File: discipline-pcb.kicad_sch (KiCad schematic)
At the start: 143 parts, among them SW1 KEYSW, SW10 KEYSW, SW11 KEYSW, SW12 KEYSW, SW13 KEYSW, SW14 KEYSW, SW16 KEYSW, SW17 KEYSW, SW18 KEYSW, SW19 KEYSW, SW2 KEYSW, SW20 KEYSW, SW21 KEYSW, SW22 KEYSW, SW23 KEYSW, SW24 KEYSW, SW25 KEYSW, SW26 KEYSW, SW27 KEYSW, SW28 KEYSW, SW29 KEYSW, SW3 KEYSW, SW31 KEYSW, SW32 KEYSW, SW33 KEYSW, SW34 KEYSW, SW35 KEYSW, SW36 KEYSW, SW37 KEYSW, SW38 KEYSW, SW39 KEYSW, SW4 KEYSW, SW40 KEYSW, SW41 KEYSW, SW42 KEYSW, SW43 KEYSW, SW45 KEYSW, SW46 KEYSW, SW47 KEYSW, SW48 KEYSW, SW49 KEYSW, SW5 KEYSW, SW50 KEYSW, SW51 KEYSW, SW52 KEYSW, SW53 KEYSW, SW54 KEYSW, SW55 KEYSW, SW56 KEYSW, SW57 KEYSW, SW59 KEYSW, SW6 KEYSW, SW60 KEYSW, SW61 KEYSW, SW62 KEYSW, SW7 KEYSW, SW72 KEYSW, SW73 KEYSW, SW74 KEYSW, SW75 KEYSW, SW76 KEYSW, SW77 KEYSW, SW78 KEYSW, SW79 KEYSW, SW8 KEYSW, SW80 KEYSW, SW81 KEYSW, SW82 KEYSW, SW83 KEYSW, SW9 KEYSW

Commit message: add dru
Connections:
- net col0: now also A1.20 (GPIO15); no longer A1.26 (GPIO20)
- net col1: now also A1.19 (GPIO14); no longer A1.25 (GPIO19)
- net col10: now also A1.7 (GPIO5); no longer A1.14 (GPIO10)
- net col11: now also A1.6 (GPIO4); no longer A1.12 (GPIO9)
- net col12: now also A1.5 (GPIO3); no longer A1.11 (GPIO8)
- net col13: now also A1.21 (GPIO16); no longer A1.10 (GPIO7)
- net col14: now also A1.4 (GPIO2); no longer A1.9 (GPIO6)
- net col15: now also A1.2 (GPIO1); no longer A1.7 (GPIO5)
- net col16: now also A1.1 (GPIO0); no longer A1.6 (GPIO4)
- net col2: now also A1.17 (GPIO13); no longer A1.24 (GPIO18)
- net col3: now also A1.16 (GPIO12); no longer A1.22 (GPIO17)
- net col4: now also A1.15 (GPIO11); no longer A1.21 (GPIO16)
- net col5: now also A1.14 (GPIO10); no longer A1.20 (GPIO15)
- net col6: now also A1.12 (GPIO9); no longer A1.19 (GPIO14)
- net col7: now also A1.11 (GPIO8); no longer A1.17 (GPIO13)
- net col8: now also A1.10 (GPIO7); no longer A1.16 (GPIO12)
- net col9: now also A1.9 (GPIO6); no longer A1.15 (GPIO11)
- net row0: now also A1.32 (GPIO27_ADC1); no longer A1.34 (GPIO28_ADC2)
- net row1: now also A1.31 (GPIO26_ADC0); no longer A1.32 (GPIO27_ADC1)
- net row2: now also A1.27 (GPIO21); no longer A1.31 (GPIO26_ADC0)
- net row3: now also A1.34 (GPIO28_ADC2); no longer A1.29 (GPIO22)
- net row4: now also A1.29 (GPIO22); no longer A1.27 (GPIO21)

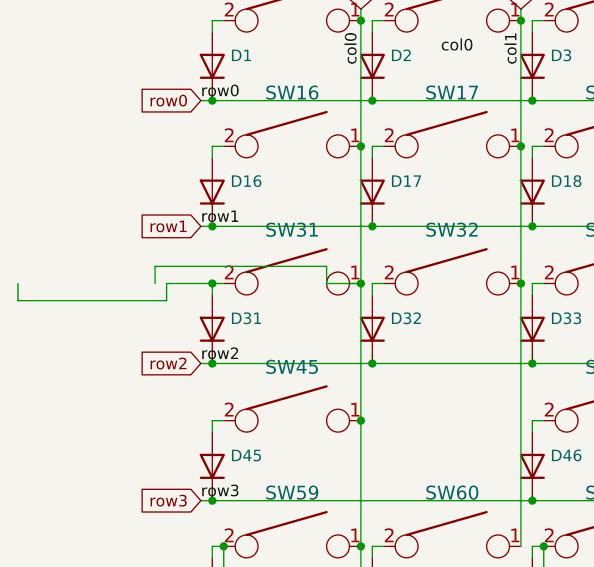
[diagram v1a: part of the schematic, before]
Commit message: update to hotswap; needs rerouting
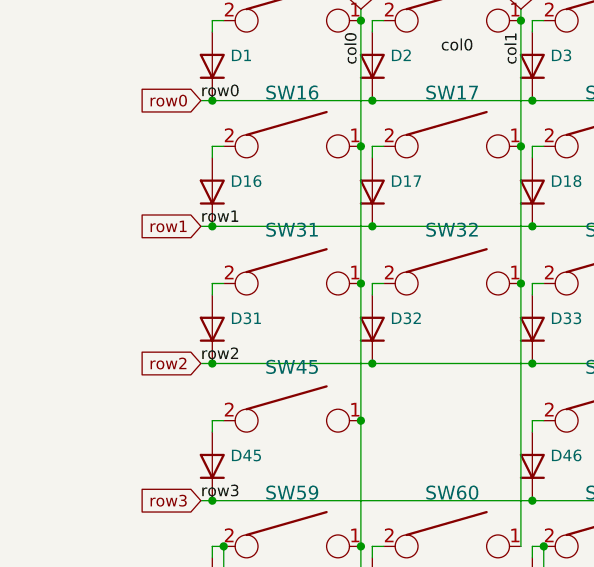
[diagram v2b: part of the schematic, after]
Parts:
- SW1, SW10, SW11, SW12, SW13, SW17, SW18, SW19, SW2, SW20, SW21, SW22, SW23, SW24, SW25, SW26, SW27, SW28, SW3, SW32, SW33, SW34, SW35, SW36, SW37, SW38, SW39, SW4, SW40, SW41, SW42, SW46, SW47, SW48, SW49, SW5, SW50, SW51, SW52, SW53, SW54, SW55, SW6, SW7, SW72, SW75, SW76, SW77, SW78, SW79, SW8, SW80, SW81, SW82, SW83, SW9: footprint cftkb:SW_Cherry_MX1A_1.00u_PCB-NOSCREEN -> MX_Hotswap:MX-Hotswap-1U
- SW14: footprint cftkb:SW_Cherry_MX1A_2.00u_PCBNOSCREEN -> MX_Hotswap:MX-Hotswap-2U
- SW16, SW29, SW73, SW74: footprint cftkb:SW_Cherry_MX1A_1.50u_PCBNOSCREEN -> MX_Hotswap:MX-Hotswap-1.5U
- SW31: footprint cftkb:SW_Cherry_MX1A_1.75u_PCBNOSCREEN -> MX_Hotswap:MX-Hotswap-1.75U
- SW43, SW45: footprint cftkb:SW_Cherry_MX1A_2.25u_PCBNOSCREEN -> MX_Hotswap:MX-Hotswap-2.25U
- SW56: footprint cftkb:SW_Cherry_MX1A_2.75u_PCB_NOSCREEN -> MX_Hotswap:MX-Hotswap-2.75U
- SW57, SW59, SW60, SW61: footprint cftkb:SW_Cherry_MX1A_1.25u_PCBNOSCREEN -> MX_Hotswap:MX-Hotswap-1.25U
- SW62: footprint cftkb:SW_Cherry_MX1A_1.00u_PCB-NOSCREEN -> MX_Hotswap:MX-Hotswap-7U-ReversedStabilizers

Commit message: add level shifter for a laugh
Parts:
- added SW-RST1: EVQ, Button_Switch_SMD:Panasonic_EVQPUM_EVQPUD, symbol Switch:SW_Push
- added U1: SN74AHCT125N, footprints:N14, symbol discipline-lib:SN74AHCT125N
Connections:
- net +5V: now also U1.14 (VCC)
- net GND: now also SW-RST1.2, U1.1 (*1OE), U1.7 (GND)
- net ledpin: now reaches A1.22 (GPIO17)
- net ledpin: now also U1.2 (1A)
- net Resetbtn: now reaches A1.30 (RUN)
- net Resetbtn: now also SW-RST1.1
- net VSYS: now reaches A1.39 (VSYS)
- new net led5vout: U1.3 (1Y)
- no-connect marks 2 -> 1

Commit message: add decoupling caps
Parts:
- added C1, C10, C11, C12, C13, C14, C15, C16, C17, C18, C19, C2, C20, C21, C22, C23, C24, C25, C26, C27, C28, C29, C3, C30, C4, C5, C6, C7, C8, C9: 100nF 0603, Capacitor_SMD:C_0603_1608Metric_Pad1.08x0.95mm_HandSolder, symbol Device:C_Small
- added D100, D15, D30, D44, D58, D63, D64, D65, D66, D67, D68, D69, D70, D71, D84, D85, D86, D87, D88, D89, D90, D91, D92, D93, D94, D95, D96, D97, D98, D99: WS2812B, LED_SMD:LED_WS2812B_PLCC4_5.0x5.0mm_P3.2mm, symbol LED:WS2812B
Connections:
- net GND: now also C1.2, C10.2, C11.2, C12.2, C13.2, C14.2, C15.2, C16.2, C17.2, C18.2, C19.2, C2.2, C20.2, C21.2, C22.2, C23.2, C24.2, C25.2, C26.2, C27.2, C28.2, C29.2, C3.2, C30.2, C4.2, C5.2, C6.2, C7.2, C8.2, C9.2, D100.3 (VSS), D15.3 (VSS), D30.3 (VSS), D44.3 (VSS), D58.3 (VSS), D63.3 (VSS), D64.3 (VSS), D65.3 (VSS), D66.3 (VSS), D67.3 (VSS), D68.3 (VSS), D69.3 (VSS), D70.3 (VSS), D71.3 (VSS), D84.3 (VSS), D85.3 (VSS), D86.3 (VSS), D87.3 (VSS), D88.3 (VSS), D89.3 (VSS), D90.3 (VSS), D91.3 (VSS), D92.3 (VSS), D93.3 (VSS), D94.3 (VSS), D95.3 (VSS), D96.3 (VSS), D97.3 (VSS), D98.3 (VSS), D99.3 (VSS)
- net VSYS: now also C1.1, C10.1, C11.1, C12.1, C13.1, C14.1, C15.1, C16.1, C17.1, C18.1, C19.1, C2.1, C20.1, C21.1, C22.1, C23.1, C24.1, C25.1, C26.1, C27.1, C28.1, C29.1, C3.1, C30.1, C4.1, C5.1, C6.1, C7.1, C8.1, C9.1, D100.1 (VDD), D15.1 (VDD), D30.1 (VDD), D44.1 (VDD), D58.1 (VDD), D63.1 (VDD), D64.1 (VDD), D65.1 (VDD), D66.1 (VDD), D67.1 (VDD), D68.1 (VDD), D69.1 (VDD), D70.1 (VDD), D71.1 (VDD), D84.1 (VDD), D85.1 (VDD), D86.1 (VDD), D87.1 (VDD), D88.1 (VDD), D89.1 (VDD), D90.1 (VDD), D91.1 (VDD), D92.1 (VDD), D93.1 (VDD), D94.1 (VDD), D95.1 (VDD), D96.1 (VDD), D97.1 (VDD), D98.1 (VDD), D99.1 (VDD)
- net led5vout: now also D15.4 (DIN)
- new net: D100.4 (DIN), D99.2 (DOUT)
- new net: D98.2 (DOUT), D99.4 (DIN)
- new net: D94.2 (DOUT), D95.4 (DIN)
- new net: D93.2 (DOUT), D94.4 (DIN)
- new net: D44.2 (DOUT), D58.4 (DIN)
- new net: D30.2 (DOUT), D44.4 (DIN)
- new net: D86.2 (DOUT), D87.4 (DIN)
- new net: D85.2 (DOUT), D86.4 (DIN)
- new net: D89.2 (DOUT), D90.4 (DIN)
- new net: D88.2 (DOUT), D89.4 (DIN)
- new net: D84.2 (DOUT), D85.4 (DIN)
- new net: D71.2 (DOUT), D84.4 (DIN)
- new net: D15.2 (DOUT), D30.4 (DIN)
- new net: D69.4 (DIN), D70.2 (DOUT)
- new net: D64.2 (DOUT), D70.4 (DIN)
- new net: D90.2 (DOUT), D91.4 (DIN)
- new net: D92.2 (DOUT), D93.4 (DIN)
- new net: D96.2 (DOUT), D97.4 (DIN)
- new net: D95.2 (DOUT), D96.4 (DIN)
- new net: D63.2 (DOUT), D64.4 (DIN)
- new net: D87.2 (DOUT), D88.4 (DIN)
- new net: D65.4 (DIN), D66.2 (DOUT)
- new net: D66.4 (DIN), D67.2 (DOUT)
- new net: D97.2 (DOUT), D98.4 (DIN)
- new net: D58.2 (DOUT), D63.4 (DIN)
- new net: D67.4 (DIN), D68.2 (DOUT)
- new net: D91.2 (DOUT), D92.4 (DIN)
- new net: D68.4 (DIN), D69.2 (DOUT)
- new net: D65.2 (DOUT), D71.4 (DIN)
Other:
- moved on the sheet: A1, D1, D10, D11, D12, D13, D14, D16, D17, D18, D19, D2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

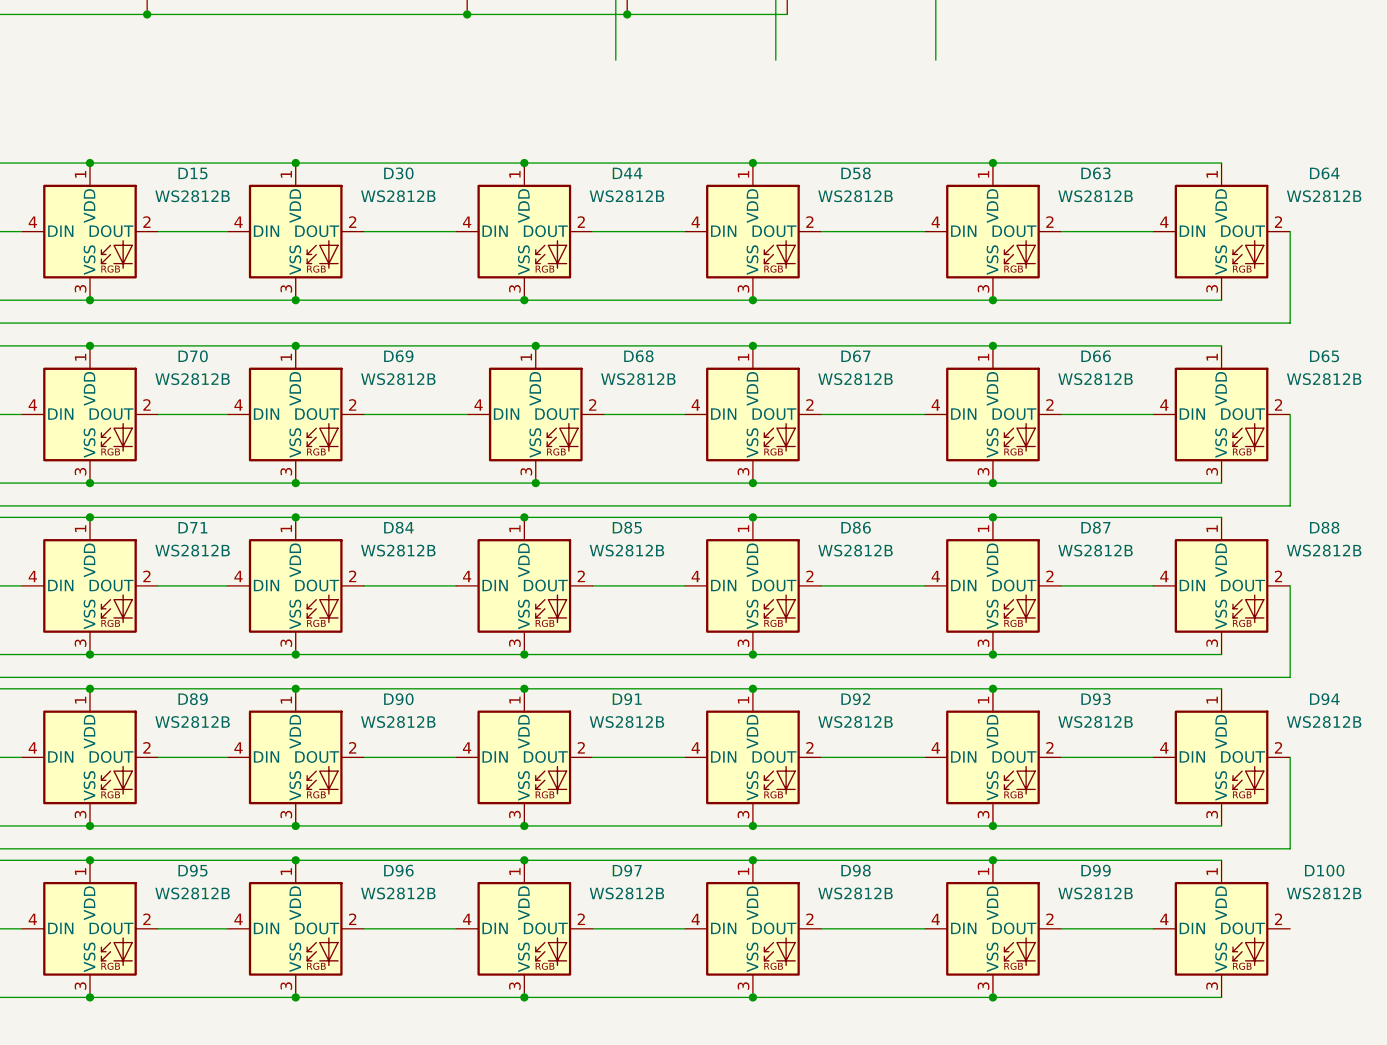
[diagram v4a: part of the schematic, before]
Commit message: update led labels
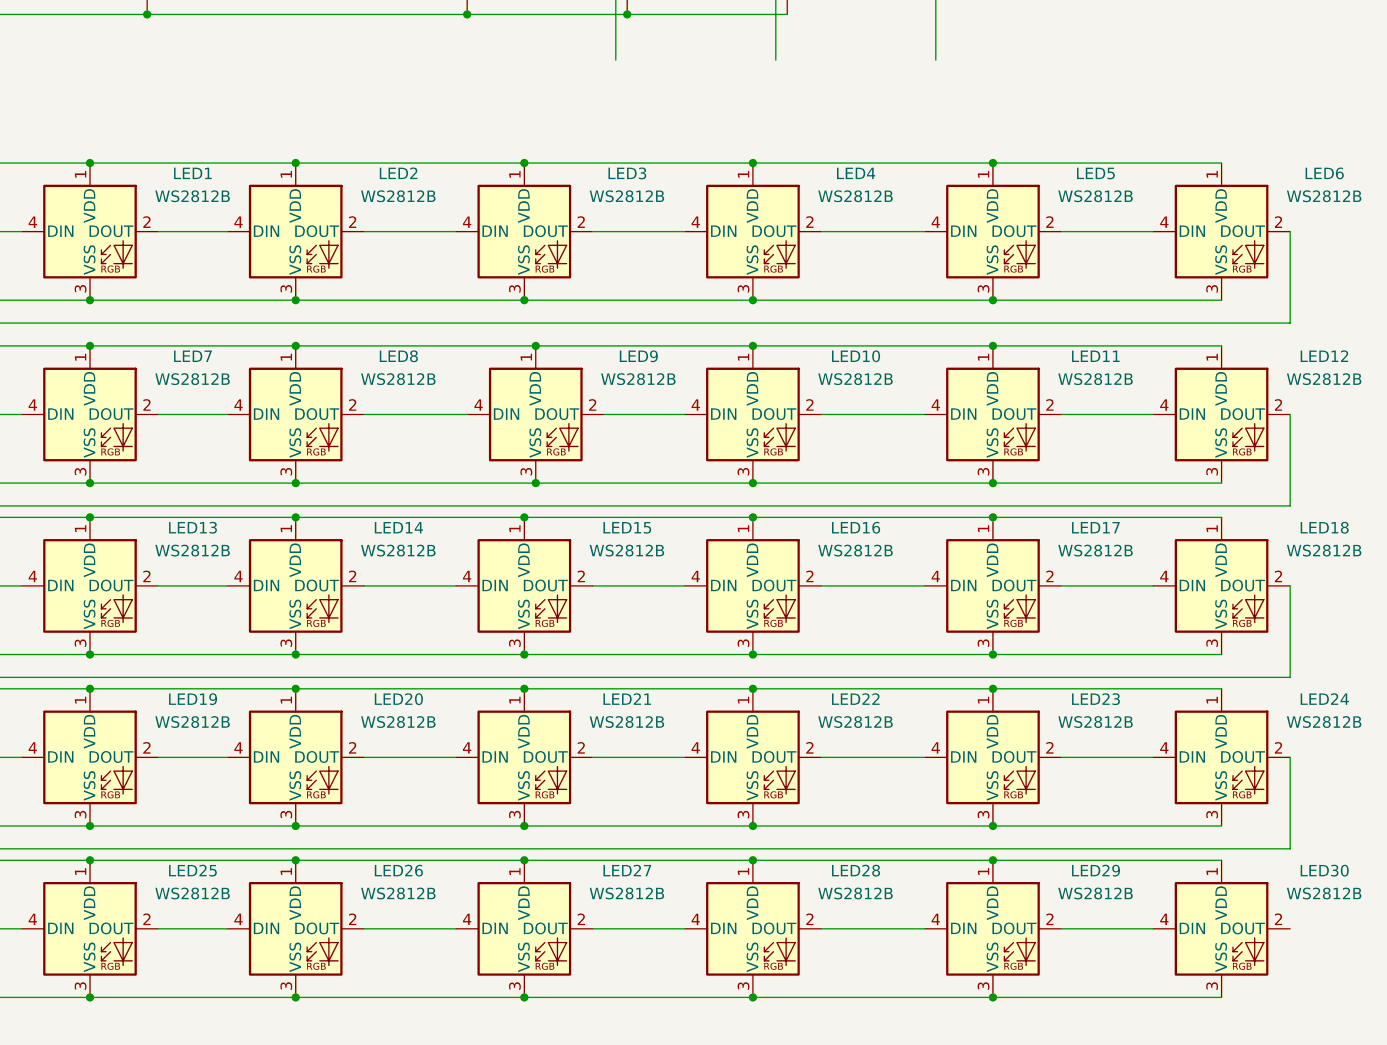
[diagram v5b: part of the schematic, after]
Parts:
- renumbered D15 to LED1, D67 to LED10, D66 to LED11, D65 to LED12, D71 to LED13, D84 to LED14, D85 to LED15, D86 to LED16, D87 to LED17, D88 to LED18, D89 to LED19, D30 to LED2, D90 to LED20, D91 to LED21, D92 to LED22, D93 to LED23, D94 to LED24, D95 to LED25, D96 to LED26, D97 to LED27, D98 to LED28, D99 to LED29, D44 to LED3, D100 to LED30, D58 to LED4, D63 to LED5, D64 to LED6, D70 to LED7, D69 to LED8, D68 to LED9
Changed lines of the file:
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@@
 		(dnp no)
 		(fields_autoplaced yes)
-		(property "Reference" "D99"
+		(property "Reference" "LED29"
 			(at 365.76 190.4298 0)
 			(effects
@@
 			(project "discipline-pcb"
 				(path "/92ddd8bc-b115-4355-8708-2687f9ad53cd"
-					(reference "D99")
+					(reference "LED29")
 					(unit 1)
 				)
@@
 		(dnp no)
 		(fields_autoplaced yes)
-		(property "Reference" "D94"
+		(property "Reference" "LED24"
 			(at 391.16 171.3798 0)
 			(effects
@@
 			(project "discipline-pcb"
 				(path "/92ddd8bc-b115-4355-8708-2687f9ad53cd"
-					(reference "D94")
+					(reference "LED24")
 					(unit 1)
 				)
@@
 		(dnp no)
 		(fields_autoplaced yes)
-		(property "Reference" "D44"
+		(property "Reference" "LED3"
 			(at 313.69 112.9598 0)
 			(effects
@@
 			(project "discipline-pcb"
 				(path "/92ddd8bc-b115-4355-8708-2687f9ad53cd"
-					(reference "D44")
+					(reference "LED3")
 					(unit 1)
 				)
@@
 		(dnp no)
 		(fields_autoplaced yes)
-		(property "Reference" "D86"
+		(property "Reference" "LED16"
 			(at 339.09 152.3298 0)
 			(effects
@@
 			(project "discipline-pcb"
 				(path "/92ddd8bc-b115-4355-8708-2687f9ad53cd"
-					(reference "D86")
+					(reference "LED16")
 					(unit 1)
 				)
@@
 		(dnp no)
 		(fields_autoplaced yes)
-		(property "Reference" "D89"
+		(property "Reference" "LED19"
 			(at 265.43 171.3798 0)
 			(effects
@@
 			(project "discipline-pcb"
 				(path "/92ddd8bc-b115-4355-8708-2687f9ad53cd"
-					(reference "D89")
+					(reference "LED19")
 					(unit 1)
 				)
@@
 		(dnp no)
 		(fields_autoplaced yes)
-		(property "Reference" "D84"
+		(property "Reference" "LED14"
 			(at 288.29 152.3298 0)
 			(effects
@@
 			(project "discipline-pcb"
 				(path "/92ddd8bc-b115-4355-8708-2687f9ad53cd"
-					(reference "D84")
+					(reference "LED14")
 					(unit 1)
 				)
@@
 		(dnp no)
 		(fields_autoplaced yes)
-		(property "Reference" "D15"
+		(property "Reference" "LED1"
 			(at 265.43 112.9598 0)
 			(effects
@@
 			(project ""
 				(path "/92ddd8bc-b115-4355-8708-2687f9ad53cd"
-					(reference "D15")
+					(reference "LED1")
 					(unit 1)
 				)
@@
 		(dnp no)
 		(fields_autoplaced yes)
-		(property "Reference" "D100"
+		(property "Reference" "LED30"
 			(at 391.16 190.4298 0)
 			(effects
@@
 			(project "discipline-pcb"
 				(path "/92ddd8bc-b115-4355-8708-2687f9ad53cd"
-					(reference "D100")
+					(reference "LED30")
 					(unit 1)
 				)
@@
 		(dnp no)
 		(fields_autoplaced yes)
-		(property "Reference" "D70"
+		(property "Reference" "LED7"
 			(at 265.43 133.2798 0)
 			(effects
@@
 			(project "discipline-pcb"
 				(path "/92ddd8bc-b115-4355-8708-2687f9ad53cd"
-					(reference "D70")
+					(reference "LED7")
 					(unit 1)
 				)
@@
 		(dnp no)
 		(fields_autoplaced yes)
-		(property "Reference" "D90"
+		(property "Reference" "LED20"
 			(at 288.29 171.3798 0)
 			(effects
@@
 			(project "discipline-pcb"
 				(path "/92ddd8bc-b115-4355-8708-2687f9ad53cd"
-					(reference "D90")
+					(reference "LED20")
 					(unit 1)
 				)
@@
 		(dnp no)
 		(fields_autoplaced yes)
-		(property "Reference" "D93"
+		(property "Reference" "LED23"
 			(at 365.76 171.3798 0)
 			(effects
@@
 			(project "discipline-pcb"
 				(path "/92ddd8bc-b115-4355-8708-2687f9ad53cd"
-					(reference "D93")
+					(reference "LED23")
 					(unit 1)
 				)
@@
 		(dnp no)
 		(fields_autoplaced yes)
-		(property "Reference" "D96"
+		(property "Reference" "LED26"
 			(at 288.29 190.4298 0)
 			(effects
@@
 			(project "discipline-pcb"
 				(path "/92ddd8bc-b115-4355-8708-2687f9ad53cd"
-					(reference "D96")
+					(reference "LED26")
 					(unit 1)
 				)
@@
 		(dnp no)
 		(fields_autoplaced yes)
-		(property "Reference" "D64"
+		(property "Reference" "LED6"
 			(at 391.16 112.9598 0)
 			(effects
@@
 			(project "discipline-pcb"
 				(path "/92ddd8bc-b115-4355-8708-2687f9ad53cd"
-					(reference "D64")
+					(reference "LED6")
 					(unit 1)
 				)
@@
 		(dnp no)
 		(fields_autoplaced yes)
-		(property "Reference" "D87"
+		(property "Reference" "LED17"
 			(at 365.76 152.3298 0)
 			(effects
@@
 			(project "discipline-pcb"
 				(path "/92ddd8bc-b115-4355-8708-2687f9ad53cd"
-					(reference "D87")
+					(reference "LED17")
 					(unit 1)
 				)
@@
 		(dnp no)
 		(fields_autoplaced yes)
-		(property "Reference" "D66"
+		(property "Reference" "LED11"
 			(at 365.76 133.2798 0)
 			(effects
@@
 			(project "discipline-pcb"
 				(path "/92ddd8bc-b115-4355-8708-2687f9ad53cd"
-					(reference "D66")
+					(reference "LED11")
 					(unit 1)
 				)
@@
 		(dnp no)
 		(fields_autoplaced yes)
-		(property "Reference" "D98"
+		(property "Reference" "LED28"
 			(at 339.09 190.4298 0)
 			(effects
@@
 			(project "discipline-pcb"
 				(path "/92ddd8bc-b115-4355-8708-2687f9ad53cd"
-					(reference "D98")
+					(reference "LED28")
 					(unit 1)
 				)
@@
 		(dnp no)
 		(fields_autoplaced yes)
-		(property "Reference" "D63"
+		(property "Reference" "LED5"
 			(at 365.76 112.9598 0)
 			(effects
@@
 			(project "discipline-pcb"
 				(path "/92ddd8bc-b115-4355-8708-2687f9ad53cd"
-					(reference "D63")
+					(reference "LED5")
 					(unit 1)
 				)
@@
 		(dnp no)
 		(fields_autoplaced yes)
-		(property "Reference" "D67"
+		(property "Reference" "LED10"
 			(at 339.09 133.2798 0)
 			(effects
@@
 			(project "discipline-pcb"
 				(path "/92ddd8bc-b115-4355-8708-2687f9ad53cd"
-					(reference "D67")
+					(reference "LED10")
 					(unit 1)
 				)
@@
 		(dnp no)
 		(fields_autoplaced yes)
-		(property "Reference" "D58"
+		(property "Reference" "LED4"
 			(at 339.09 112.9598 0)
 			(effects
@@
 			(project "discipline-pcb"
 				(path "/92ddd8bc-b115-4355-8708-2687f9ad53cd"
-					(reference "D58")
+					(reference "LED4")
 					(unit 1)
 				)
@@
 		(dnp no)
 		(fields_autoplaced yes)
-		(property "Reference" "D85"
+		(property "Reference" "LED15"
 			(at 313.69 152.3298 0)
 			(effects
@@
 			(project "discipline-pcb"
 				(path "/92ddd8bc-b115-4355-8708-2687f9ad53cd"
-					(reference "D85")
+					(reference "LED15")
 					(unit 1)
 				)
@@
 		(dnp no)
 		(fields_autoplaced yes)
-		(property "Reference" "D97"
+		(property "Reference" "LED27"
 			(at 313.69 190.4298 0)
 			(effects
@@
 			(project "discipline-pcb"
 				(path "/92ddd8bc-b115-4355-8708-2687f9ad53cd"
-					(reference "D97")
+					(reference "LED27")
 					(unit 1)
 				)
@@
 		(dnp no)
 		(fields_autoplaced yes)
-		(property "Reference" "D92"
+		(property "Reference" "LED22"
 			(at 339.09 171.3798 0)
 			(effects
@@
 			(project "discipline-pcb"
 				(path "/92ddd8bc-b115-4355-8708-2687f9ad53cd"
-					(reference "D92")
+					(reference "LED22")
 					(unit 1)
 				)
@@
 		(dnp no)
 		(fields_autoplaced yes)
-		(property "Reference" "D91"
+		(property "Reference" "LED21"
 			(at 313.69 171.3798 0)
 			(effects
@@
 			(project "discipline-pcb"
 				(path "/92ddd8bc-b115-4355-8708-2687f9ad53cd"
-					(reference "D91")
+					(reference "LED21")
 					(unit 1)
 				)
@@
 		(dnp no)
 		(fields_autoplaced yes)
-		(property "Reference" "D69"
+		(property "Reference" "LED8"
 			(at 288.29 133.2798 0)
 			(effects
@@
 			(project "discipline-pcb"
 				(path "/92ddd8bc-b115-4355-8708-2687f9ad53cd"
-					(reference "D69")
+					(reference "LED8")
 					(unit 1)
 				)
@@
 		(dnp no)
 		(fields_autoplaced yes)
-		(property "Reference" "D95"
+		(property "Reference" "LED25"
 			(at 265.43 190.4298 0)
 			(effects
@@
 			(project "discipline-pcb"
 				(path "/92ddd8bc-b115-4355-8708-2687f9ad53cd"
-					(reference "D95")
+					(reference "LED25")
 					(unit 1)
 				)
@@
 		(dnp no)
 		(fields_autoplaced yes)
-		(property "Reference" "D88"
+		(property "Reference" "LED18"
 			(at 391.16 152.3298 0)
 			(effects
@@
 			(project "discipline-pcb"
 				(path "/92ddd8bc-b115-4355-8708-2687f9ad53cd"
-					(reference "D88")
+					(reference "LED18")
 					(unit 1)
 				)
@@
 		(dnp no)
 		(fields_autoplaced yes)
-		(property "Reference" "D30"
+		(property "Reference" "LED2"
 			(at 288.29 112.9598 0)
 			(effects
@@
 			(project "discipline-pcb"
 				(path "/92ddd8bc-b115-4355-8708-2687f9ad53cd"
-					(reference "D30")
+					(reference "LED2")
 					(unit 1)
 				)
@@
 		(dnp no)
 		(fields_autoplaced yes)
-		(property "Reference" "D71"
+		(property "Reference" "LED13"
 			(at 265.43 152.3298 0)
 			(effects
@@
 			(project "discipline-pcb"
 				(path "/92ddd8bc-b115-4355-8708-2687f9ad53cd"
-					(reference "D71")
+					(reference "LED13")
 					(unit 1)
 				)
@@
 		(dnp no)
 		(fields_autoplaced yes)
-		(property "Reference" "D68"
+		(property "Reference" "LED9"
 			(at 314.96 133.2798 0)
 			(effects
@@
 			(project "discipline-pcb"
 				(path "/92ddd8bc-b115-4355-8708-2687f9ad53cd"
-					(reference "D68")
+					(reference "LED9")
 					(unit 1)
 				)
@@
 		(dnp no)
 		(fields_autoplaced yes)
-		(property "Reference" "D65"
+		(property "Reference" "LED12"
 			(at 391.16 133.2798 0)
 			(effects
@@
 			(project "discipline-pcb"
 				(path "/92ddd8bc-b115-4355-8708-2687f9ad53cd"
-					(reference "D65")
+					(reference "LED12")
 					(unit 1)
 				)

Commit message: add leds to pcb
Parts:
- renumbered LED1 to LED_5V1
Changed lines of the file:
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@@
 		(on_board yes)
 		(dnp no)
-		(property "Reference" "LED1"
+		(property "Reference" "LED_5V1"
 			(at 49.53 180.34 0)
 			(effects
@@
 			(project ""
 				(path "/92ddd8bc-b115-4355-8708-2687f9ad53cd"
-					(reference "LED1")
+					(reference "LED_5V1")
 					(unit 1)
 				)
